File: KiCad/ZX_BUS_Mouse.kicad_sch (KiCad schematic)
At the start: 31 parts, among them J1 X1A, J2 X1B, J3 UART, J4 Mini-DIN-6, J5 ISP, J6 Debug, J7 JTAG, J8 PS/2 External Bracket, U1 ATmega8A-A, U2 EPM3032ALC44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

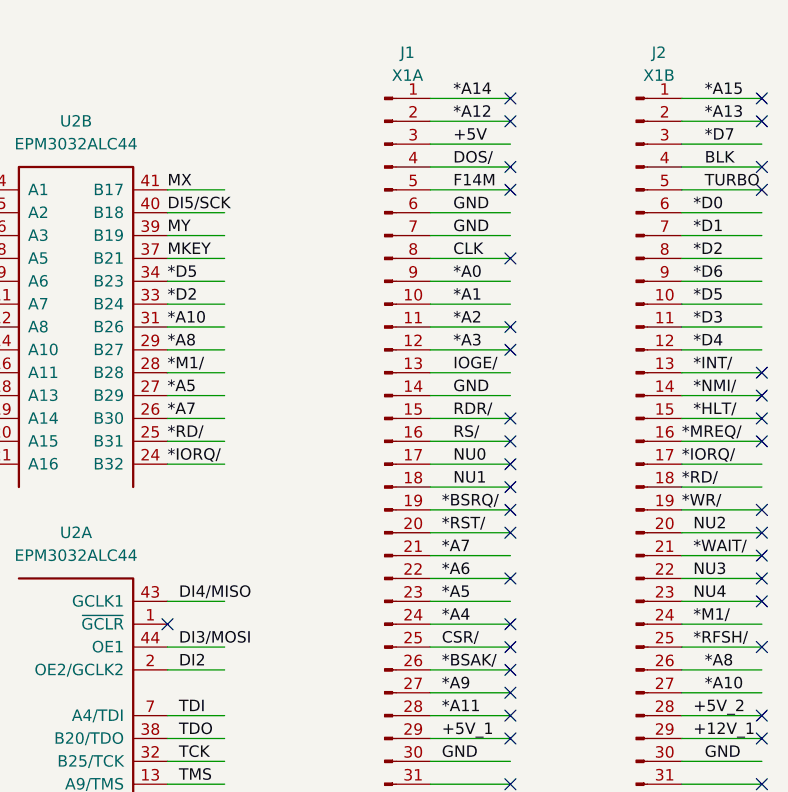
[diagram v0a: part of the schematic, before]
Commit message: Scorpion ZS 256 Service ROM / ProfROM by @LW_aka_PLM: fixed ROM Disk loading with mouse enabled. Added A15 to IORQGE / ports addresses decode.
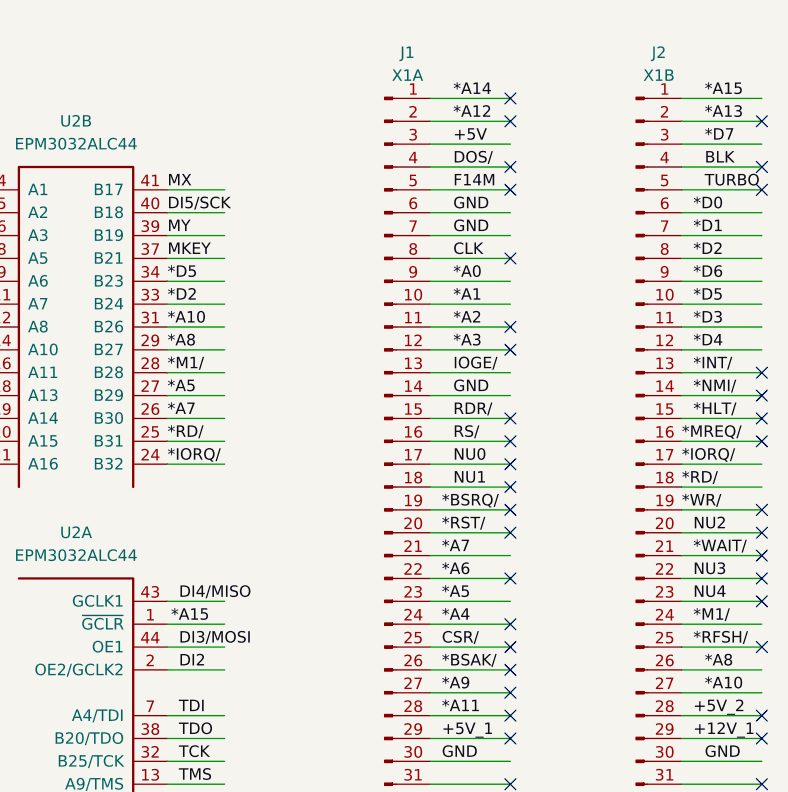
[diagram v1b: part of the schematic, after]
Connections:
- net *A15: now also U2.1 (~{GCLR})
- no-connect marks 55 -> 53
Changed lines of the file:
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@@
   (no_connect (at 223.52 35.56))
   (no_connect (at 223.52 101.6))
-  (no_connect (at 223.52 25.4))
   (no_connect (at 113.03 52.07))
   (no_connect (at 223.52 76.2))
@@
   (no_connect (at 195.58 86.36))
   (no_connect (at 195.58 50.8))
-  (no_connect (at 157.48 83.82))
   (no_connect (at 223.52 27.94))
   (no_connect (at 195.58 71.12))
@@
     (stroke (width 0) (type default))
   )
+  (wire (pts (xy 157.48 83.82) (xy 163.83 83.82))
+    (stroke (width 0) (type default))
+  )
   (wire (pts (xy 76.2 46.99) (xy 83.82 46.99))
     (stroke (width 0) (type default))
@@
     (effects (font (size 1.27 1.27)) (justify left bottom))
   )
+  (label "*A15" (at 157.861 83.82 0) (fields_autoplaced)
+    (effects (font (size 1.27 1.27)) (justify left bottom))
+  )
